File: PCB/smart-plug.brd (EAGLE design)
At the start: 66 x 65.7 mm, 15 parts, among them K1 HLS8L-DC3V-S-C, T1 2N2222, X3 OUT-3PINS

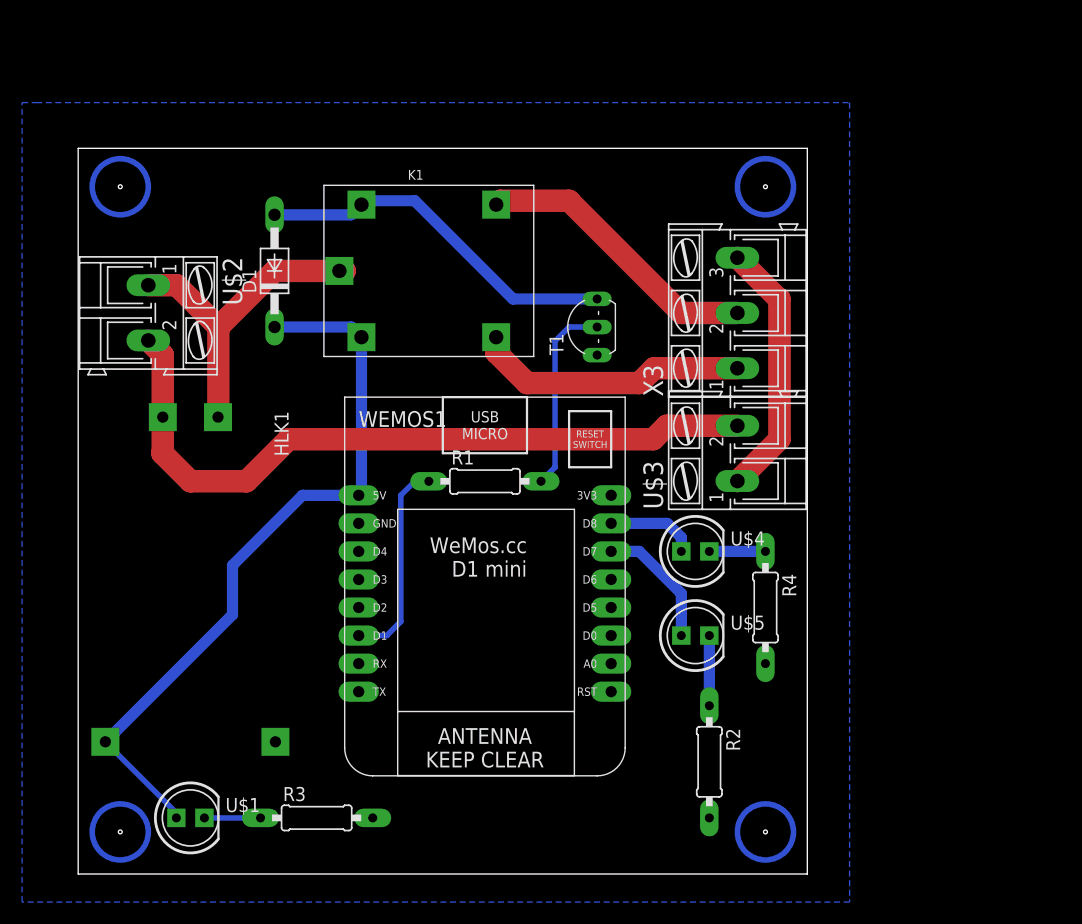
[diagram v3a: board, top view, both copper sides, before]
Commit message: Update PCB files
Improved design, added SMD components and current sensor
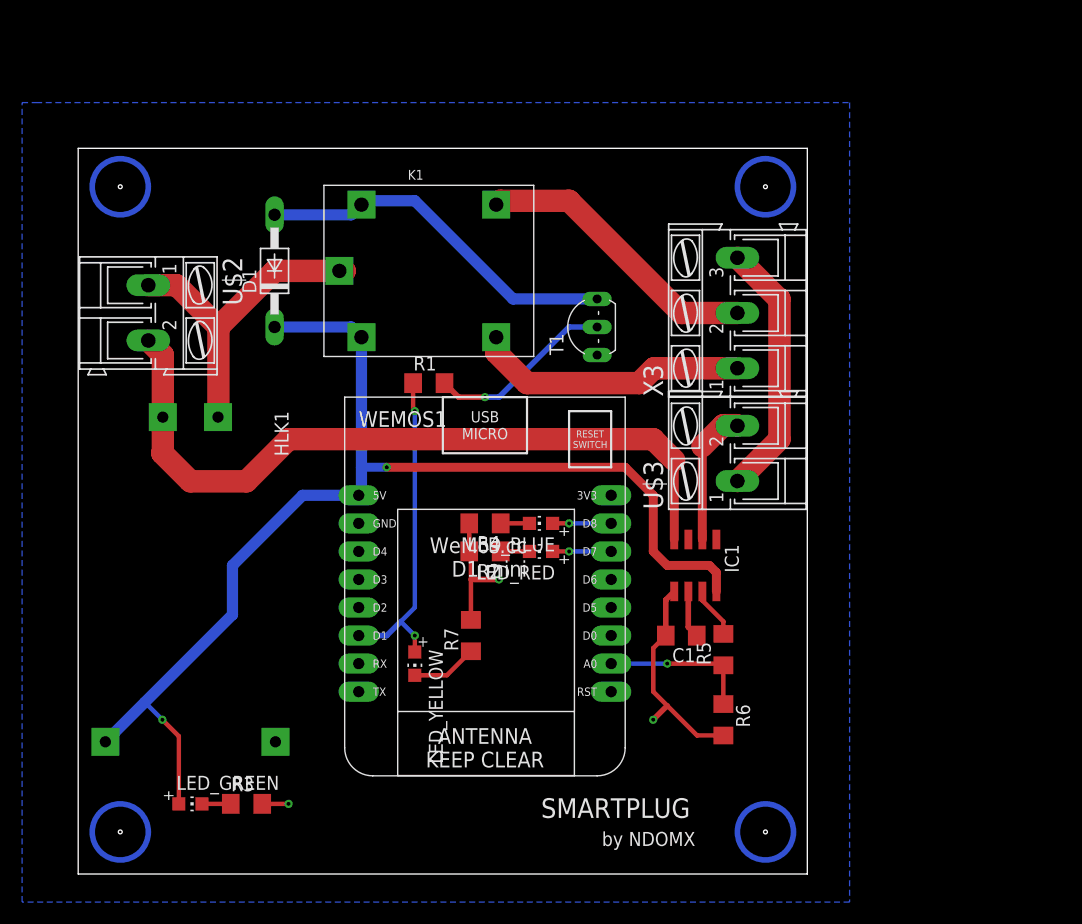
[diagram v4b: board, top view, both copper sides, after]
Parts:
- removed U$1, U$4, U$5: LED5MM, smartplug-components:LED5MM
- added C1: 1nF, adafruit:C1206
- added IC1: ACS712, ACS712:SO08
- added LED_BLUE, LED_GREEN, LED_RED, LED_YELLOW: (no value), adafruit:CHIP-LED0805
- added R5: 10k, adafruit:R1206
- added R6: 22k, adafruit:R1206
- added R7: 470, adafruit:R1206
- R1: value RESISTOR -> 10k; device smartplug-components:0207/10 -> adafruit:R1206
- R2, R3, R4: value RESISTOR -> 470; device smartplug-components:0207/10 -> adafruit:R1206
- moved R2 27.9 mm to (47.0, 29.2), turned to 180 degrees
- moved R4 26.5 mm to (47.0, 31.8), turned to 180 degrees
- moved R1 10.2 mm to (41.9, 44.5)
- moved R3 6.48 mm to (25.4, 6.35)
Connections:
- new net LED_GREEN1: LED_YELLOW.C, R7.1
- new net N$1: IC1.2, U$3.2
- new net N$5: C1.1, IC1.6
- new net N$7: IC1.7, R5.2
- new net N$8: R5.1, R6.1, WEMOS1.A0
- net 220V-: now also IC1.4; no longer U$3.2
- net AGND: now also C1.2, IC1.5, R6.2, R7.2
- net LED_BLUE: now also LED_BLUE.A; no longer U$4.A
- net LED_GREEN: now also LED_GREEN.C; no longer U$1.K
- net LED_RED: now also LED_RED.A; no longer U$5.A
- net N$10: now also LED_BLUE.C; no longer U$4.K
- net N$2: now also LED_YELLOW.A
- net N$4: now also IC1.8, LED_GREEN.A; no longer U$1.A
- net N$9: now also LED_RED.C; no longer U$5.K
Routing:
- net N$4: track 67.0 -> 108.7 mm, vias 0 -> 2
- net AGND: track 0.00 -> 33.4 mm, vias 0 -> 3
- net N$8: track 0.00 -> 13.7 mm, vias 0 -> 1
- net N$1: track 0.00 -> 12.4 mm
- net N$2: track 18.8 -> 29.8 mm, vias 0 -> 2
- net LED_RED: track 11.7 -> 5.30 mm, vias 0 -> 1
- net LED_GREEN1: track 0.00 -> 5.98 mm
- net N$7: track 0.00 -> 4.64 mm
- net N$5: track 0.00 -> 4.32 mm
- net N$9: track 6.35 -> 2.61 mm
- net LED_BLUE: track 8.15 -> 5.30 mm, vias 0 -> 1
- net LED_GREEN: track 5.08 -> 2.61 mm
- net N$10: track 5.08 -> 2.61 mm
- net 220V-: track 66.0 -> 67.7 mm
- net N$3: track 17.6 -> 17.0 mm, vias 0 -> 1
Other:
- board text added: "SMARTPLUG"
- board text added: "YELLOW"
- board text added: "by NDOMX"
